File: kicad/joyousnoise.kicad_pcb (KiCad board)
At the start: 2 copper layers, 10 parts, among them P1 Power, P2 Speaker, U1 40106

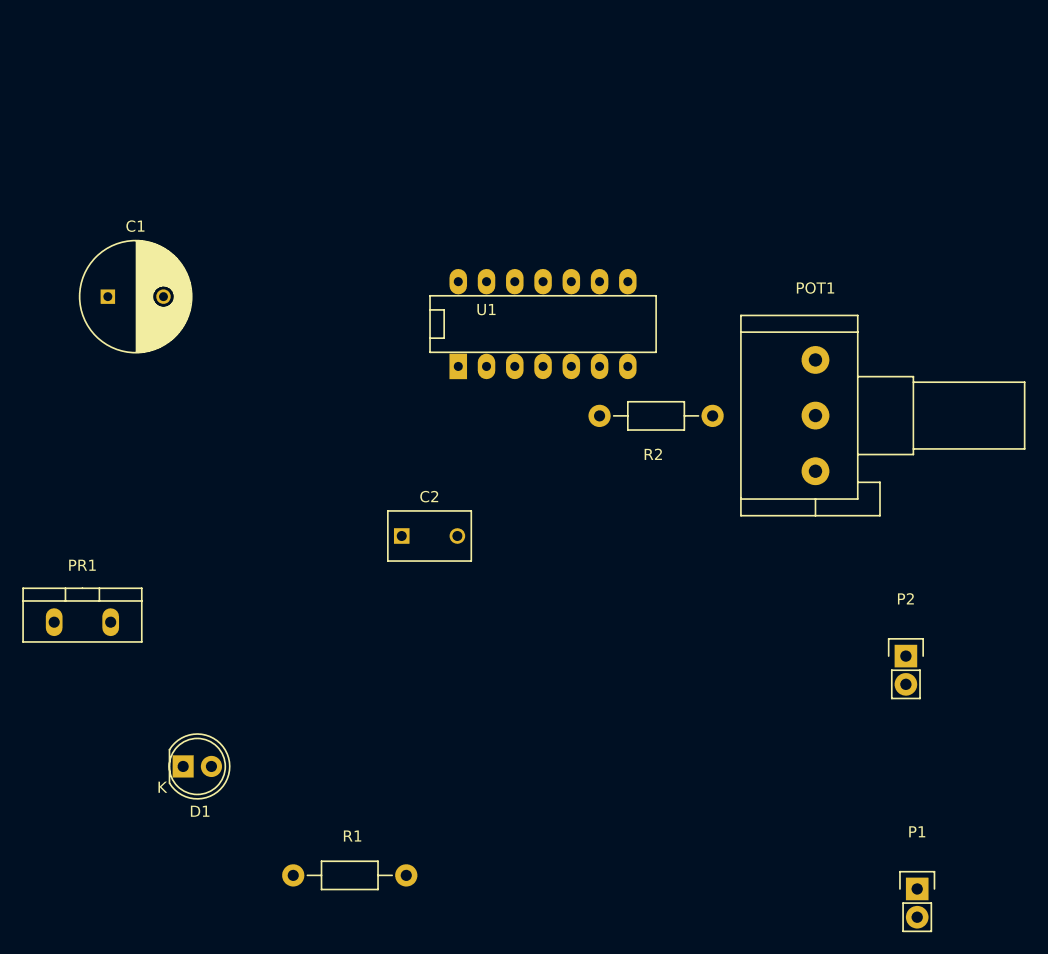
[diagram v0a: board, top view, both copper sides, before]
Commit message: redo lost work, add power switch
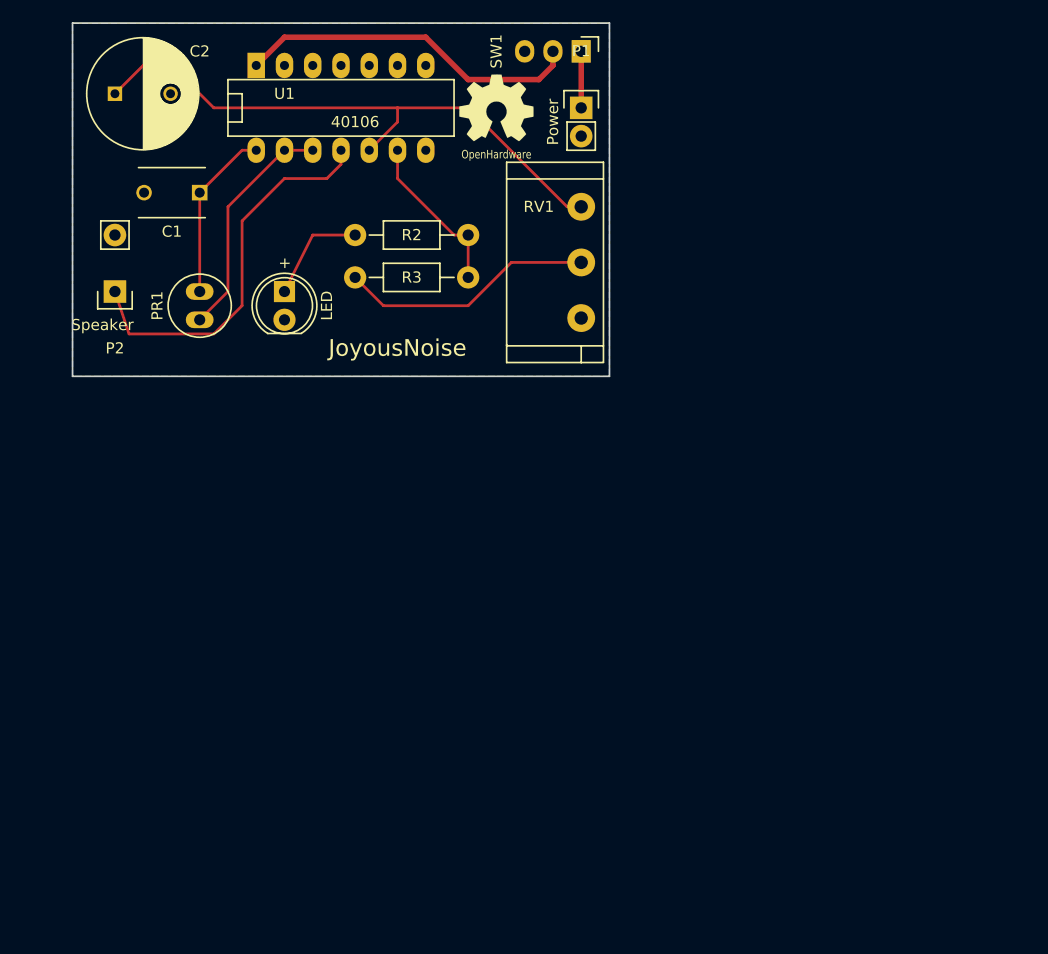
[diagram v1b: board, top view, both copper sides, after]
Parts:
- removed POT1: POT, Potentiometers:Potentiometer_Alps-RK16-single
- removed R1: R, Resistors_ThroughHole:Resistor_Horizontal_RM10mm
- added G***: LOGO, lib:OSHW_6mm, B.Cu at (149.9, 58.4)
- added G***: LOGO, lib:OSHW_6mm, F.Cu at (149.9, 58.4)
- added R3: R, lib:Resistor_Horizontal_RM10mm, F.Cu at (142.2, 73.7)
- added RV1: POT, lib:Potentiometer_Alps-RK16-single, F.Cu at (157.5, 67.3)
- added SW1: SPST, lib:SM_SlideSW, F.Cu at (157.5, 53.3)
- C1: footprint Capacitors_ThroughHole:C_Radial_D10_L20_P5 -> lib:C_Disc_D6_P5
- C2: value C -> CP; footprint Capacitors_ThroughHole:C_Disc_D7.5_P5 -> lib:C_Radial_D10_L20_P5
- D1: footprint LEDs:LED-5MM -> lib:LED-5MM
- P1: footprint Pin_Headers:Pin_Header_Straight_1x02 -> lib:Pin_Header_Straight_1x02
- P2: footprint Pin_Headers:Pin_Header_Straight_1x02 -> lib:Speaker_conn
- PR1: footprint Resistors_ThroughHole:Resistor_TO-220_Vertical -> lib:PhotoResistor
- R2: footprint Resistors_ThroughHole:Resistor_Horizontal_RM10mm -> lib:Resistor_Horizontal_RM10mm
- U1: footprint Sockets_DIP:DIP-14__300_ELL -> lib:DIP-14__300_ELL
- moved P2 78.3 mm to (115.6, 74.9), turned to 180 degrees
- moved P1 76.4 mm to (157.5, 58.4)
- moved C2 47.4 mm to (115.6, 57.1)
- moved D1 41.2 mm to (130.8, 77.5), turned to 90 degrees
- moved PR1 30.3 mm to (123.2, 76.2), turned to 90 degrees
- moved R2 27.3 mm to (142.2, 69.8), turned to 0 degrees
- moved U1 26.6 mm to (135.9, 58.4)
- moved C1 12.5 mm to (123.2, 66.0), turned to 180 degrees
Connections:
- C2 pad 2: Net-(C2-Pad2) -> GND
- P1 pad 1: VCC -> Net-(P1-Pad1)
- P2 pad 1: Net-(P2-Pad1) -> /OUT
- PR1 pad 2: Net-(PR1-Pad2) -> Net-(C1-Pad1)
- R2 pad 1: Net-(POT1-Pad2) -> Net-(D1-Pad2)
- U1 pad 1: Net-(U1-Pad1) -> Net-(C1-Pad1)
- U1 pad 14: GND -> VCC
- U1 pad 2: Net-(U1-Pad2) -> Net-(PR1-Pad1)
- U1 pad 4: Net-(U1-Pad4) -> /OUT
- U1 pad 5: Net-(POT1-Pad1) -> Net-(C2-Pad1)
- U1 pad 7: VCC -> GND
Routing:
- net Net-(C2-Pad1): track 0.00 -> 53.1 mm
- net /OUT: track 0.00 -> 35.1 mm
- net VCC: track 0.00 -> 31.1 mm
- net Net-(R3-Pad1): track 0.00 -> 23.0 mm
- net Net-(PR1-Pad1): track 0.00 -> 20.9 mm
- net Net-(C1-Pad1): track 0.00 -> 15.5 mm
- net Net-(R2-Pad2): track 0.00 -> 14.8 mm
- net Net-(D1-Pad2): track 0.00 -> 9.49 mm
- net Net-(P1-Pad1): track 0.00 -> 5.08 mm
- added copper zone on B.Cu, net GND
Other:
- board outline added: 48.3 x 31.8 mm
- net class PowerNets added: clearance 0.25, trace_width 0.5, via_dia 0.6, via_drill 0.4
- board text added: "JoyousNoise"
- board text added: "JoyousNoise HTTP://baldwisdom.com"

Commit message: update silkscreen
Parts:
- C1: footprint lib:C_Disc_D6_P5 -> C_Disc_D6_P5
- C2: footprint lib:C_Radial_D10_L20_P5 -> C_Radial_D10_L20_P5
- moved P2 1.80 mm to (114.3, 76.2)
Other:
- board text added: "+"
